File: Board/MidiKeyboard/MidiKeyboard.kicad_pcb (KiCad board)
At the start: 2 copper layers, 201.2 x 67 mm, 161 parts, among them J1 USB_C_Receptacle_16P, J2 Bat, Q1 DMP3099L, SW1 CK_KMS2xxG, SW10 SW_Push_45deg, SW11 SW_Push_45deg, SW12 SW_Push_45deg, SW13 SW_Push_45deg, SW14 SW_Push_45deg, SW15 SW_Push_45deg, SW16 SW_Push_45deg, SW17 SW_Push_45deg, SW18 SW_Push_45deg, SW19 SW_Push_45deg, SW2 SW_Push_45deg, SW20 SW_Push_45deg, SW21 SW_Push_45deg, SW22 SW_Push_45deg, SW23 SW_Push_45deg, SW24 SW_Push_45deg, SW25 SW_Push_45deg, SW26 SW_Push_45deg, SW27 SW_Push_45deg, SW28 SW_Push_45deg, SW29 SW_Push_45deg, SW3 SW_Push_45deg, SW30 SW_Push_45deg, SW31 SW_Push_45deg, SW32 SW_Push_45deg, SW33 SW_Push_45deg, SW34 SW_Push_45deg, SW35 SW_Push_45deg, SW36 SW_Push_45deg, SW37 SW_Push_45deg, SW38 SW_Push_45deg, SW39 SW_Push_45deg, SW4 SW_Push_45deg, SW40 SW_Push_45deg, SW41 SW_Push_45deg, SW42 SW_Push_45deg, SW43 SW_Push_45deg, SW44 SW_Push_45deg, SW45 SW_Push_45deg, SW46 SW_Push_45deg, SW47 SW_Push_45deg, SW48 SW_Push_45deg, SW49 SW_Push_45deg, SW5 SW_Push_45deg, SW50 SW_Push_45deg, SW51 SW_Push_45deg, SW52 SW_Push_45deg, SW53 SW_Push_45deg, SW54 SW_Push_45deg, SW55 SW_Push_45deg, SW56 SW_Push_45deg, SW57 SW_Push_45deg, SW58 SW_Push_45deg, SW59 SW_Push_45deg, SW6 SW_Push_45deg, SW60 SW_Push_45deg, SW61 SW_Push_45deg, SW62 SW_Push_45deg, SW63_BL1 SW_Push_45deg, SW66 RESET, SW7 SW_Push_45deg, SW8 SW_Push_45deg, SW9 SW_Push_45deg, U1 ESP32-C3, U2 XC6220B331MR, U3 TP4056-42-ESOP8, U4 TCA8418RTWR

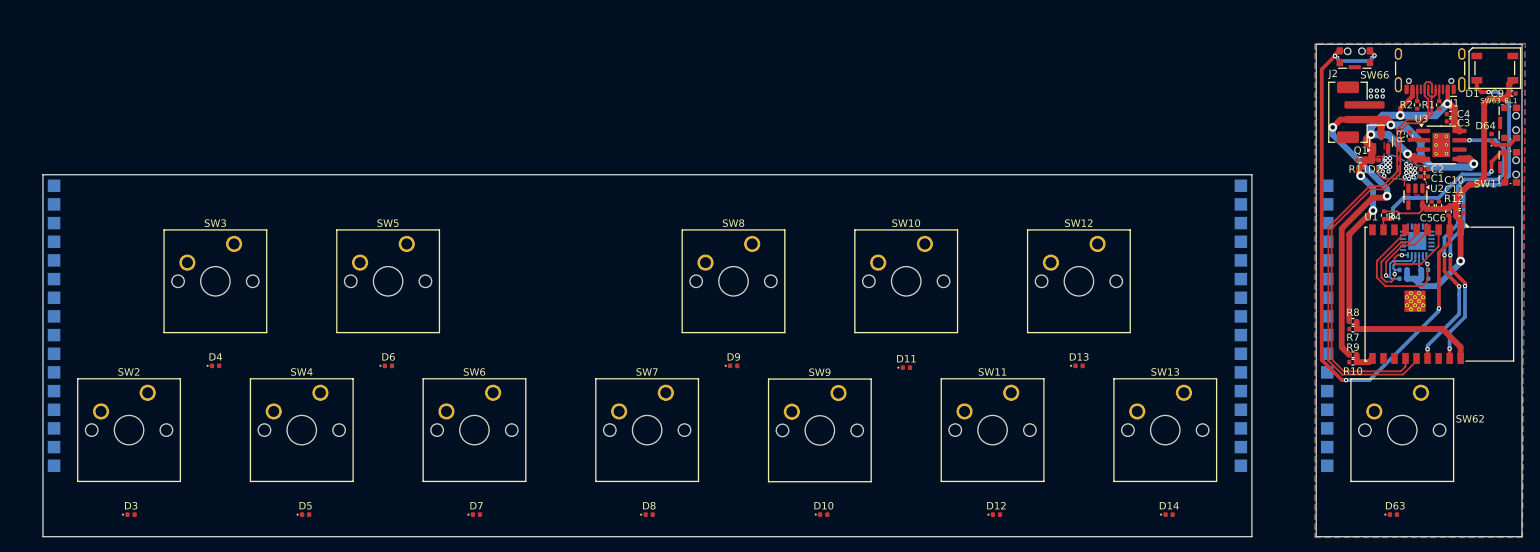
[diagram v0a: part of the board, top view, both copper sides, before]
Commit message: Main Board conections
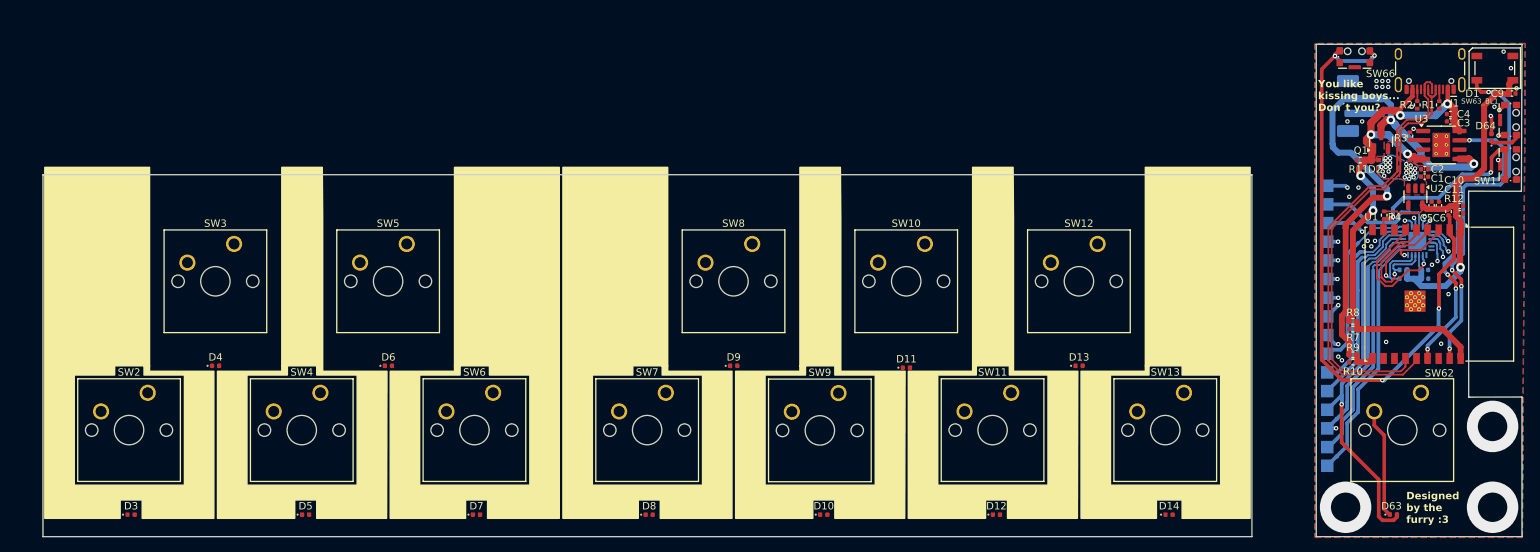
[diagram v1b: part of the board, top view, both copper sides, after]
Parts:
- J2: moved to B.Cu
- moved J2 0.85 mm to (146.8, 48.9), turned to -90 degrees
- moved SW63_BL1 0.40 mm to (167.2, 50.8)
- moved SW1 0.40 mm to (167.2, 56.9)
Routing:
- net /Switches/R5: track 0.00 -> 87.7 mm, vias 0 -> 2
- net /Switches/C7: track 0.00 -> 63.1 mm, vias 0 -> 4
- net /Switches/R4: track 0.00 -> 50.8 mm, vias 0 -> 1
- net /Switches/R7: track 0.00 -> 34.0 mm
- net /Switches/R6: track 0.00 -> 32.5 mm
- net /Switches/R3: track 0.00 -> 27.4 mm
- net /Switches/R2: track 0.00 -> 26.5 mm
- net /Switches/R1: track 0.00 -> 25.3 mm
- net /Switches/R0: track 0.00 -> 24.3 mm, vias 0 -> 2
- net /Switches/C6: track 0.00 -> 23.0 mm, vias 0 -> 2
- net /Switches/C5: track 0.00 -> 23.0 mm, vias 0 -> 2
- net /Switches/C4: track 0.00 -> 20.9 mm, vias 0 -> 2
- net /Switches/C3: track 0.00 -> 18.7 mm, vias 0 -> 2
- net /Switches/C0: track 0.00 -> 17.7 mm, vias 0 -> 2
- net /Switches/C1: track 0.00 -> 16.3 mm
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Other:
- outline, holes or cut-outs redrawn
- copper layers 2 -> 4
- board text added: "Designed by the furry :3"
- board text added: "You like kissing boys... Don´t you?"
